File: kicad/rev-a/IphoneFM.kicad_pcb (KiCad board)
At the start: 2 copper layers, 46.5 x 71.4 mm, 106 parts, among them J1 USB 2.0 Type-C, J2 SMA jack, SW1 SPDT, SW2 SPST, SW3 6 × SPST, U1 MCU, U2 Synthesizer, U3 3.3 V 600 mA LDO, U4 FM receiver, U5 SPDT RF switch, U6 USB ESD array, U7 Digital step attenuator, Y2 20 MHz CMOS XO

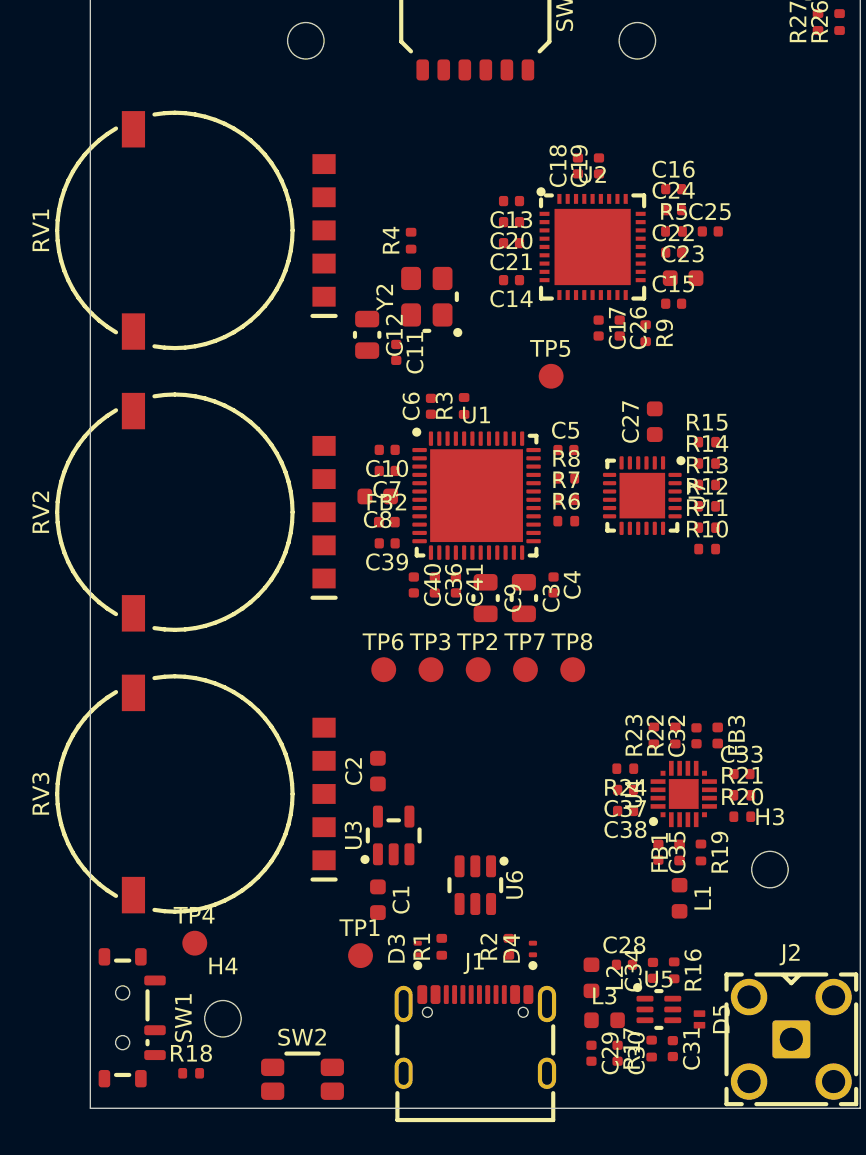
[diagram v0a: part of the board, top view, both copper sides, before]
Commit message: Step 5.1: ground fan-out, 102 vias and 106 stubs, locked (tools/pcb_fanout.py)
Co-Authored-By: Claude Opus 5.5 <noreply@anthropic.com>
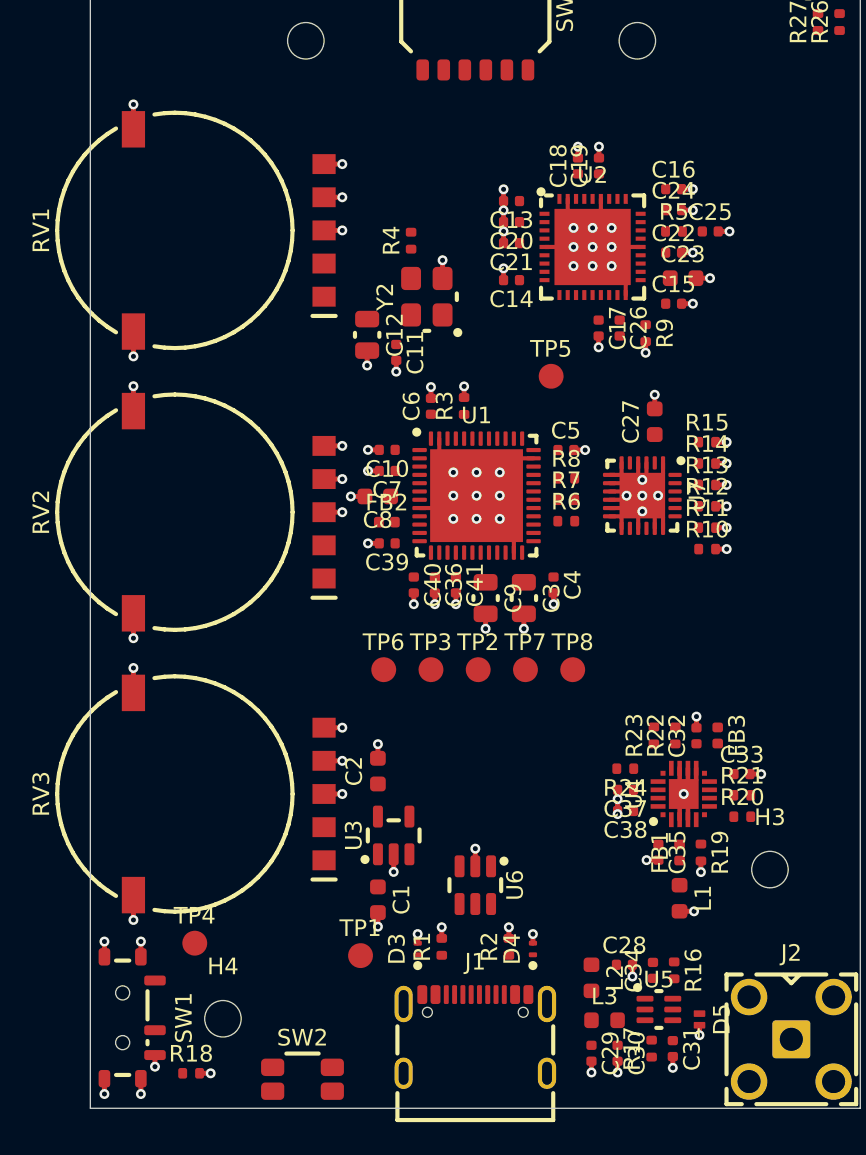
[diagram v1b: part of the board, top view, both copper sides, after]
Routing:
- net GND: track 0.00 -> 84.8 mm, vias 0 -> 102

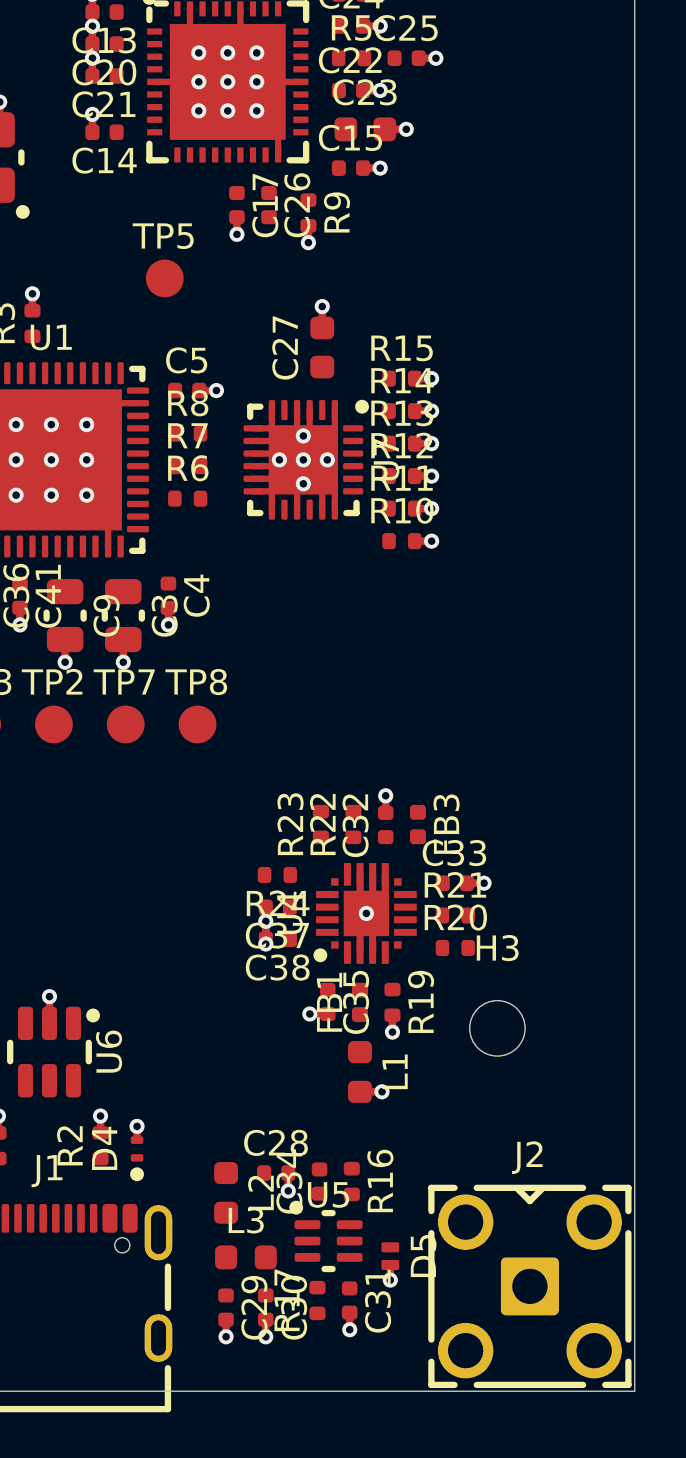
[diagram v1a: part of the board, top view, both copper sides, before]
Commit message: Steps 5.4-5.6: RF lines laid by hand and locked (tools/pcb_route_rf.py)
Co-Authored-By: Claude Opus 5.5 <noreply@anthropic.com>
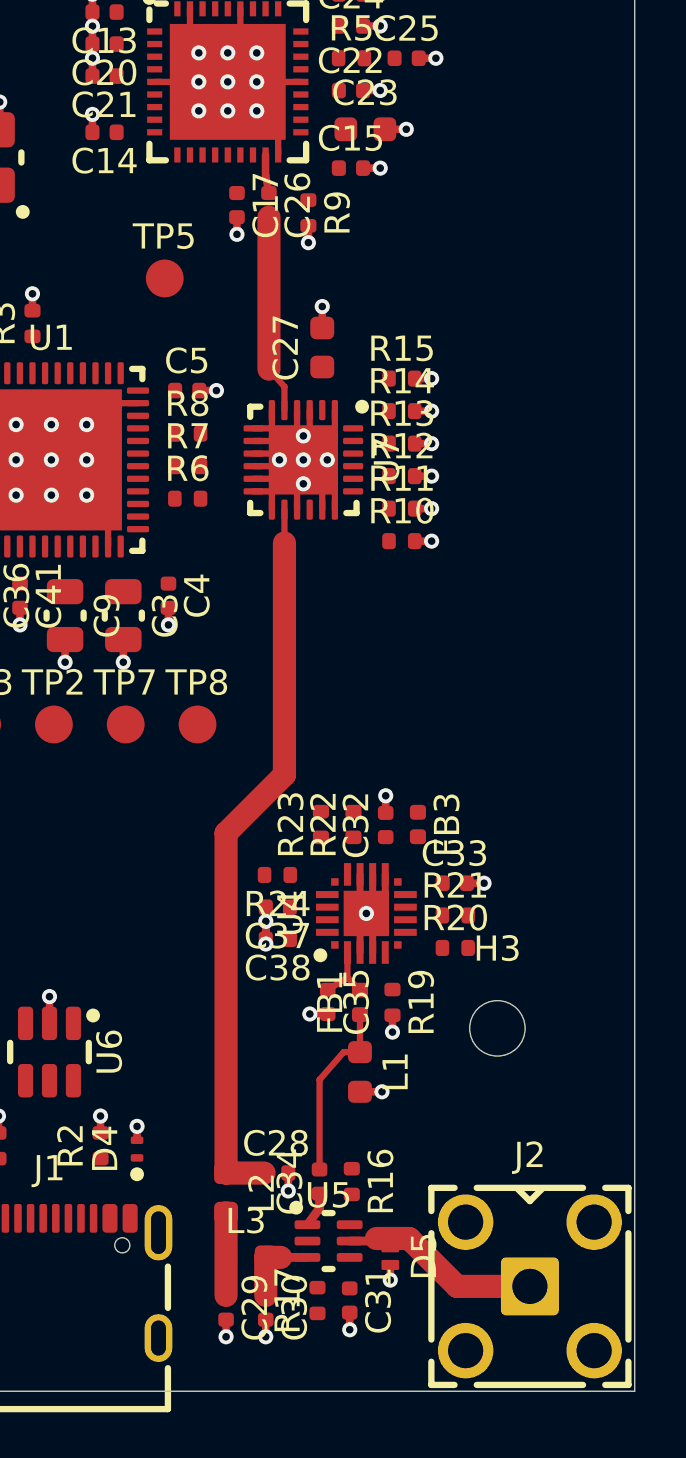
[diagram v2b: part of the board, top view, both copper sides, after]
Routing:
- net /TX_RF_ATT: track 0.00 -> 28.8 mm
- net /ANT: track 0.00 -> 7.96 mm
- net /ATT_IN: track 0.00 -> 7.89 mm
- net /FMI_MATCH: track 0.00 -> 7.15 mm
- net /TX_LPF_MID: track 0.00 -> 3.28 mm
- net /TX_RF: track 0.00 -> 3.16 mm
- net /FMI: track 0.00 -> 2.62 mm
- net /LMX_RF: track 0.00 -> 1.52 mm
- net /RX_RF: track 0.00 -> 1.39 mm
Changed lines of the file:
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@@
+	)
+	(segment
+		(start 46.642 122.16)
+		(end 46.642 118.6)
+		(width 0.25)
+		(locked yes)
+		(layer "F.Cu")
+		(net "/FMI_MATCH")
+	)
+	(segment
+		(start 46.642 118.6)
+		(end 47.6 117.502)
+		(width 0.25)
+		(locked yes)
+		(layer "F.Cu")
+		(net "/FMI_MATCH")
+	)
+	(segment
+		(start 48.247 117.502)
+		(end 48.247 116.015)
+		(width 0.25)
+		(locked yes)
+		(layer "F.Cu")
+		(net "/FMI_MATCH")
+	)
+	(segment
+		(start 47.6 117.502)
+		(end 48.247 117.502)
+		(width 0.25)
+		(locked yes)
+		(layer "F.Cu")
+		(net "/FMI_MATCH")
+	)
+	(segment
+		(start 46.967 115.03)
+		(end 47.75 114.55)
+		(width 0.25)
+		(locked yes)
+		(layer "F.Cu")
+		(net "/FMI")
+	)
+	(segment
+		(start 47.75 114.55)
+		(end 47.75 113.55)
+		(width 0.25)
+		(locked yes)
+		(layer "F.Cu")
+		(net "/FMI")
+	)
+	(segment
+		(start 48.247 115.045)
+		(end 47.75 114.55)
+		(width 0.25)
+		(locked yes)
+		(layer "F.Cu")
+		(net "/FMI")
 	)
 	(segment
@@
 		(net "GND")
 	)
+	(segment
+		(start 42.932 123.877)
+		(end 42.932 127.16)
+		(width 0.92)
+		(locked yes)
+		(layer "F.Cu")
+		(net "/TX_LPF_MID")
+	)
+	(segment
+		(start 44.508 125.65)
+		(end 45.1 125.65)
+		(width 0.92)
+		(locked yes)
+		(layer "F.Cu")
+		(net "/TX_RF")
+	)
+	(segment
+		(start 44.508 125.65)
+		(end 44.508 127.16)
+		(width 0.92)
+		(locked yes)
+		(layer "F.Cu")
+		(net "/TX_RF")
+	)
+	(segment
+		(start 45.1 125.65)
+		(end 46.163 125.65)
+		(width 0.35)
+		(locked yes)
+		(layer "F.Cu")
+		(net "/TX_RF")
+	)
+	(segment
+		(start 44.635 84.37)
+		(end 44.635 90.4)
+		(width 0.92)
+		(locked yes)
+		(layer "F.Cu")
+		(net "/ATT_IN")
+	)
+	(segment
+		(start 45.25 91.1)
+		(end 45.25 92.025)
+		(width 0.25)
+		(locked yes)
+		(layer "F.Cu")
+		(net "/ATT_IN")
+	)
+	(segment
+		(start 44.635 90.4)
+		(end 45.25 91.1)
+		(width 0.25)
+		(locked yes)
+		(layer "F.Cu")
+		(net "/ATT_IN")
+	)
+	(segment
+		(start 45.25 95.975)
+		(end 45.25 97.3)
+		(width 0.25)
+		(locked yes)
+		(layer "F.Cu")
+		(net "/TX_RF_ATT")
+	)
+	(segment
+		(start 45.25 97.3)
+		(end 45.25 106.5)
+		(width 0.92)
+		(locked yes)
+		(layer "F.Cu")
+		(net "/TX_RF_ATT")
+	)
+	(segment
+		(start 42.932 108.818)
+		(end 42.932 122.302)
+		(width 0.92)
+		(locked yes)
+		(layer "F.Cu")
+		(net "/TX_RF_ATT")
+	)
+	(segment
+		(start 45.25 106.5)
+		(end 42.932 108.818)
+		(width 0.92)
+		(locked yes)
+		(layer "F.Cu")
+		(net "/TX_RF_ATT")
+	)
+	(segment
+		(start 42.932 122.302)
+		(end 44.443 122.302)
+		(width 0.92)
+		(locked yes)
+		(layer "F.Cu")
+		(net "/TX_RF_ATT")
+	)
+	(segment
+		(start 46.163 124.35)
+		(end 46.642 123.7)
+		(width 0.35)
+		(locked yes)
+		(layer "F.Cu")
+		(net "/RX_RF")
+	)
+	(segment
+		(start 46.642 123.7)
+		(end 46.642 123.12)
+		(width 0.35)
+		(locked yes)
+		(layer "F.Cu")
+		(net "/RX_RF")
+	)
+	(segment
+		(start 48.7 125)
+		(end 48.9 124.9)
+		(width 0.35)
+		(locked yes)
+		(layer "F.Cu")
+		(net "/ANT")
+	)
+	(segment
+		(start 47.837 125)
+		(end 48.7 125)
+		(width 0.35)
+		(locked yes)
+		(layer "F.Cu")
+		(net "/ANT")
+	)
+	(segment
+		(start 50.2 124.9)
+		(end 52.1 126.8)
+		(width 0.92)
+		(locked yes)
+		(layer "F.Cu")
+		(net "/ANT")
+	)
+	(segment
+		(start 48.9 124.9)
+		(end 50.2 124.9)
+		(width 0.92)
+		(locked yes)
+		(layer "F.Cu")
+		(net "/ANT")
+	)
+	(segment
+		(start 52.1 126.8)
+		(end 54.99 126.8)
+		(width 0.92)
+		(locked yes)
+		(layer "F.Cu")
+		(net "/ANT")
+	)
+	(segment
+		(start 44.5 82.7)
+		(end 44.635 83.41)
+		(width 0.3)
+		(locked yes)
+		(layer "F.Cu")
+		(net "/LMX_RF")
+	)
+	(segment
+		(start 44.5 81.9)
+		(end 44.5 82.7)
+		(width 0.3)
+		(locked yes)
+		(layer "F.Cu")
+		(net "/LMX_RF")
+	)
 	(zone

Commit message: Step 5.7 (part): U2's loop filter routed; routing tools pcb_astar.py and pcb_freeroute.py
Co-Authored-By: Claude Opus 5.5 <noreply@anthropic.com>
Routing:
- net /CP_LOOP: track 0.00 -> 3.58 mm
- net /LOOP_RC: track 0.00 -> 1.20 mm
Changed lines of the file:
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@@
+	)
+	(segment
+		(start 48.42 78.061667)
+		(end 49.62 78.061667)
+		(width 0.2)
+		(locked yes)
+		(layer "F.Cu")
+		(net "/LOOP_RC")
 	)
 	(segment
@@
 		(net "/LMX_RF")
 	)
+	(segment
+		(start 45.95 78.06)
+		(end 47.4 78.061667)
+		(width 0.2)
+		(locked yes)
+		(layer "F.Cu")
+		(net "/CP_LOOP")
+	)
+	(segment
+		(start 45.9 78)
+		(end 46.25 78.01)
+		(width 0.2)
+		(locked yes)
+		(layer "F.Cu")
+		(net "/CP_LOOP")
+	)
+	(segment
+		(start 45.9 78)
+		(end 45.95 78.06)
+		(width 0.2)
+		(locked yes)
+		(layer "F.Cu")
+		(net "/CP_LOOP")
+	)
+	(segment
+		(start 46.25 78.01)
+		(end 47.4 76.86)
+		(width 0.2)
+		(locked yes)
+		(layer "F.Cu")
+		(net "/CP_LOOP")
+	)
+	(segment
+		(start 47.4 76.86)
+		(end 47.41 76.781667)
+		(width 0.2)
+		(locked yes)
+		(layer "F.Cu")
+		(net "/CP_LOOP")
+	)
 	(zone

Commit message: Phase 5: nudges for routing room around U1 (Y2 up 2.5 mm, TP5 beside U1, SWD pads down 3 mm); fan-out redone
Co-Authored-By: Claude Opus 5.5 <noreply@anthropic.com>
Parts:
- moved TP5 10.9 mm to (29.6, 87.0)
- moved C12 3.60 mm to (32.9, 83.7)
- moved TP2 3.00 mm to (36.1, 107.5)
- moved TP3 3.00 mm to (33.2, 107.5)
- moved TP6 3.00 mm to (30.4, 107.5)
- moved TP7 3.00 mm to (39.0, 107.5)
- moved TP8 3.00 mm to (41.8, 107.5)
- moved R4 2.50 mm to (32.0, 76.1)
- moved C11 2.50 mm to (31.2, 82.9)
- moved Y2 2.50 mm to (33.0, 79.5)
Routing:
- net 3V3: track 0.00 -> 1.10 mm, vias 0 -> 1
- net /LMX_MUX: track 0.00 -> 0.90 mm, vias 0 -> 1

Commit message: Phase 5, U1 attempt 2 (partial): Y2 beside the wheels, U2's top-left caps up 0.9 mm, U7 2 mm right with its RF segments re-laid; U1's and U2's local links, FSK lines with planned entry vias at U2; clock rule lifted inside the clock lines' end parts
Co-Authored-By: Claude Opus 5.5 <noreply@anthropic.com>
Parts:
- moved C11 2.45 mm to (28.8, 83.4)
- moved R4 2.45 mm to (29.6, 76.6)
- moved Y2 2.45 mm to (30.6, 80.0)
- moved C27 2.00 mm to (48.8, 89.5)
- moved R10 2.00 mm to (51.9, 97.2)
- moved R11 2.00 mm to (51.9, 95.9)
- moved R12 2.00 mm to (51.9, 94.6)
- moved R13 2.00 mm to (51.9, 93.4)
- moved R14 2.00 mm to (51.9, 92.1)
- moved R15 2.00 mm to (51.9, 90.8)
- moved U7 2.00 mm to (48.0, 94.0)
- moved C13 0.90 mm to (38.1, 75.3)
- moved C20 0.90 mm to (38.1, 76.6)
- moved C21 0.90 mm to (38.1, 77.9)
- moved C12 0.86 mm to (32.2, 84.2)
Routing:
- net 3V3: track 1.10 -> 23.3 mm, vias 1 -> 0
- net /FSK_CLK: track 0.00 -> 20.2 mm, vias 0 -> 2
- net /FSK_FS: track 0.00 -> 16.4 mm, vias 0 -> 2
- net /FSK_DATA: track 0.00 -> 15.5 mm, vias 0 -> 2
- net VDDA: track 0.00 -> 7.56 mm
- net GND: track 84.8 -> 80.7 mm, vias 102 -> 100
- net /NRST: track 0.00 -> 3.93 mm
- net /LMX_CE: track 0.00 -> 2.82 mm
- net /VCAP: track 0.00 -> 2.29 mm
- net /LMX_VREGVCO: track 0.00 -> 2.16 mm
- net /WHEEL2: track 0.00 -> 1.90 mm
- net /LMX_BYP1: track 0.00 -> 1.89 mm
- net /FSK_DATA_MCU: track 0.00 -> 1.79 mm
- net /FSK_CLK_MCU: track 0.00 -> 1.78 mm
- net /WHEEL3: track 0.00 -> 1.68 mm
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
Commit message: Phase 5: U1 MICROWIRE pins reordered (28 MUX, 27 CLK, 26 DATA, 25 LE, driven by GPIO) so the four lines reach U2 with no crossing; C5 and R6-R8 moved for routing room; parts provenance list; R6-R8 placement trial and board view tools
Co-Authored-By: Claude Opus 5.5 <noreply@anthropic.com>
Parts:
- moved R7 8.88 mm to (39.4, 85.6), turned to 180 degrees
- moved R6 7.61 mm to (39.4, 88.2), turned to 180 degrees
- moved R8 6.38 mm to (39.4, 86.9), turned to 180 degrees
- moved C5 0.87 mm to (41.0, 90.5), turned to 90 degrees
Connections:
- U1 pad 26: /LMX_CLK -> /LMX_DATA
- U1 pad 27: /LMX_MUX -> /LMX_CLK
- U1 pad 28: /LMX_DATA -> /LMX_MUX
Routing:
- net /FSK_CLK: track 20.2 -> 0.91 mm, vias 2 -> 1
- net /FSK_FS: track 16.4 -> 0.96 mm, vias 2 -> 1
- net /FSK_DATA: track 15.5 -> 0.85 mm, vias 2 -> 1
- net /FSK_DATA_MCU: track 1.79 -> 0.00 mm
- net /FSK_CLK_MCU: track 1.78 -> 0.00 mm
- net /FSK_FS_MCU: track 1.54 -> 0.00 mm
- net GND: track 80.7 -> 80.1 mm, vias 100 -> 98

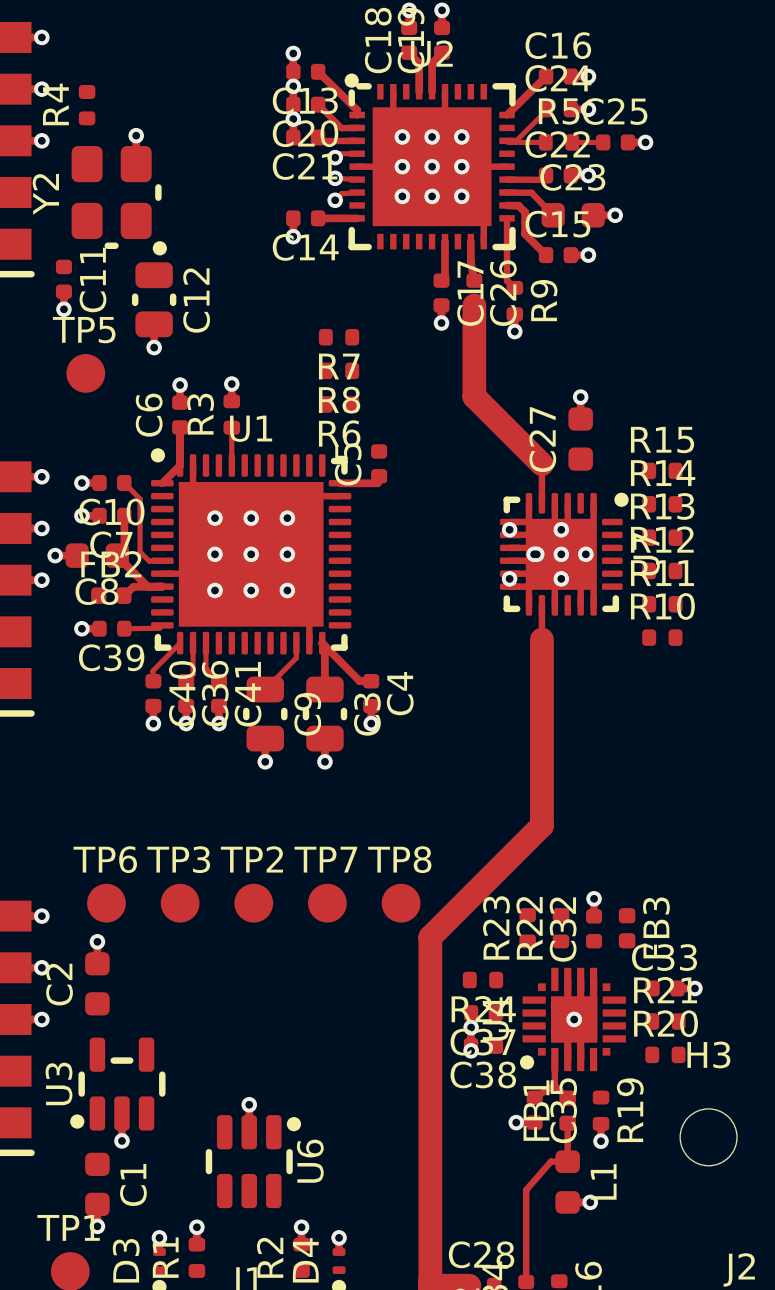
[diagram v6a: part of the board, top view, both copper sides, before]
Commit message: Phase 5: U1 right side routed: seven-line bus to U2 (MICROWIRE straight in, FSK through R6-R8 to U2's entry vias), USB and SWD crossing under it on short bottom-layer hops; U6 channels and TP7/TP8 places swapped so nothing crosses; ATT_IN bend moved toward C26; router fix (vias were placed at grid indices) and bottom-layer cost; DRC tool
Co-Authored-By: Claude Opus 5.5 <noreply@anthropic.com>
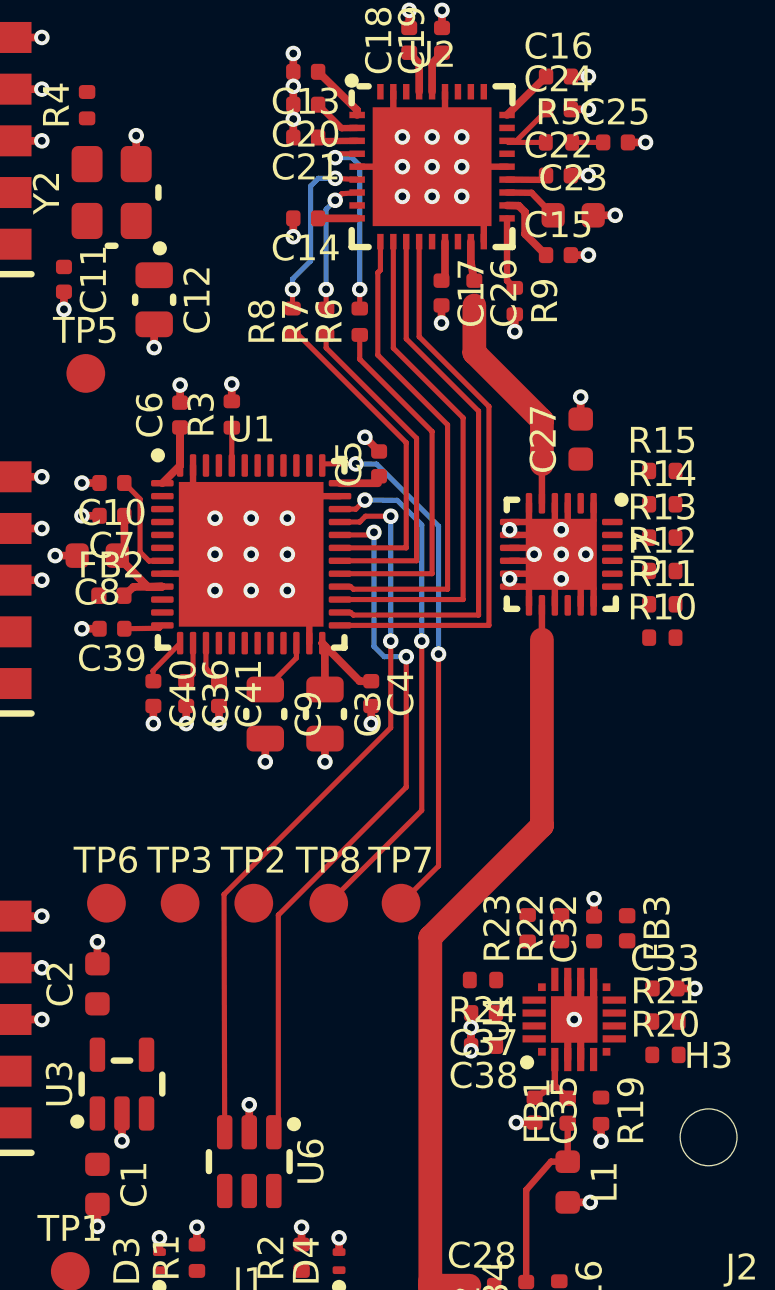
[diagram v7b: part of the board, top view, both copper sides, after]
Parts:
- moved R6 3.30 mm to (40.2, 85.0), turned to 90 degrees
- moved TP7 2.85 mm to (41.8, 107.5)
- moved TP8 2.80 mm to (39.0, 107.5)
- moved R8 2.62 mm to (37.6, 85.0), turned to 90 degrees
- moved R7 0.78 mm to (38.9, 85.0), turned to 90 degrees
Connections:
- U6 pad 1: /USB_DP -> /USB_DM
- U6 pad 3: /USB_DM -> /USB_DP
- U6 pad 4: /USB_DM -> /USB_DP
- U6 pad 6: /USB_DP -> /USB_DM
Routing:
- net /USB_DP: track 0.00 -> 28.6 mm, vias 0 -> 2
- net /USB_DM: track 0.00 -> 27.7 mm, vias 0 -> 2
- net /LMX_LE: track 0.00 -> 21.7 mm
- net /LMX_DATA: track 0.00 -> 21.0 mm
- net /SWCLK: track 0.00 -> 20.8 mm, vias 0 -> 2
- net /SWDIO: track 0.00 -> 19.8 mm, vias 0 -> 2
- net /LMX_CLK: track 0.00 -> 19.7 mm
- net /LMX_MUX: track 0.00 -> 18.8 mm
- net /FSK_CLK_MCU: track 0.00 -> 14.0 mm
- net /FSK_FS_MCU: track 0.00 -> 13.2 mm
- net /FSK_DATA_MCU: track 0.00 -> 12.8 mm
- net /FSK_CLK: track 0.91 -> 7.56 mm, vias 1 -> 2
- net /FSK_DATA: track 0.85 -> 6.99 mm, vias 1 -> 2
- net /FSK_FS: track 0.96 -> 5.32 mm, vias 1 -> 2
- net GND: track 80.1 -> 80.8 mm
